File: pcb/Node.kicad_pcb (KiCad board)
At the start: 4 copper layers, 50 x 50 mm, 164 parts, among them J1 XF2M-1415-1A, J10 BM08B-SRSS-TB, J11 BM04B-SRSS-TB, J13 SM04B-SRSS-TB, J14 BM03B-SRSS-TB, J2 USB_C_USB2.0_16P, J3 BM03B-SRSS-TB, J4 BM06B-SRSS-TB, J5 BM06B-SRSS-TB, J6 BM04B-SRSS-TB, J7 BM06B-SRSS-TB, J8 BM04B-SRSS-TB, J9 BM04B-SRSS-TB, Q1 MMBT2222A, SW1 EVQ-Q2B02W, SW2 EVQ-Q2B02W, U1 ESP32-S3-WROOM-1-N8R2, U2 LM66200DRLR, U3 USBLC6-2P6, U4 MCP23017T-E/ML, U6 LM66200DRLR, U7 AZ1084-3.3

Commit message: Updated worksheet template and logo
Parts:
- removed kibuzzard-683C4F07: G***, kibuzzard-683C4F07
- added kibuzzard-685EFB19: G***, kibuzzard-685EFB19, F.Cu at (98.5, 65.2)
- LOGO1: footprint CRGM Logos:FNWW Face 10mm -> CRGM Logos:CRGM Logo 5mm
- moved LOGO3 18.0 mm to (81.6, 65.0)
- moved LOGO1 9.38 mm to (100.1, 62.7)
- moved LOGO2 7.61 mm to (89.4, 68.4)
- moved LOGO4 0.21 mm to (101.8, 61.9)

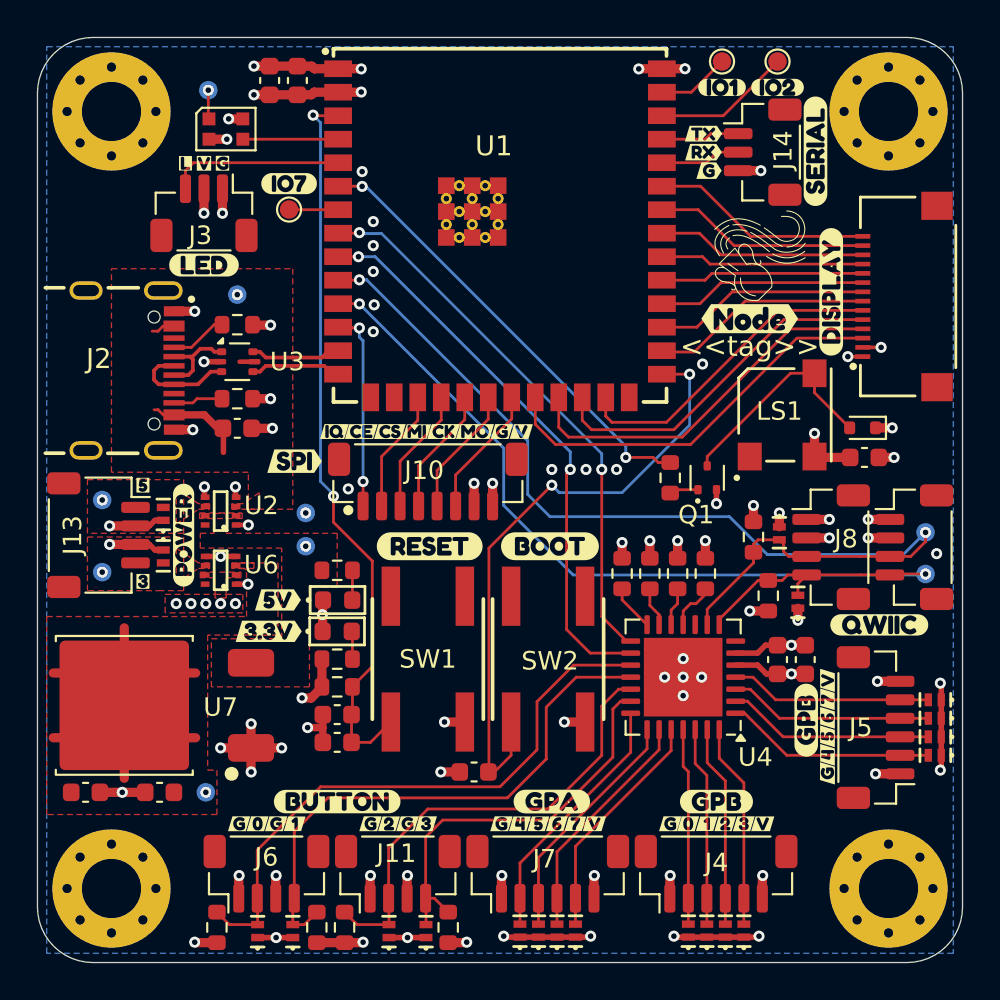
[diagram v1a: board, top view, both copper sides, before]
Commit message: Fixed footprint for Buzzer, XFC, USB ESD, and Power Switcher
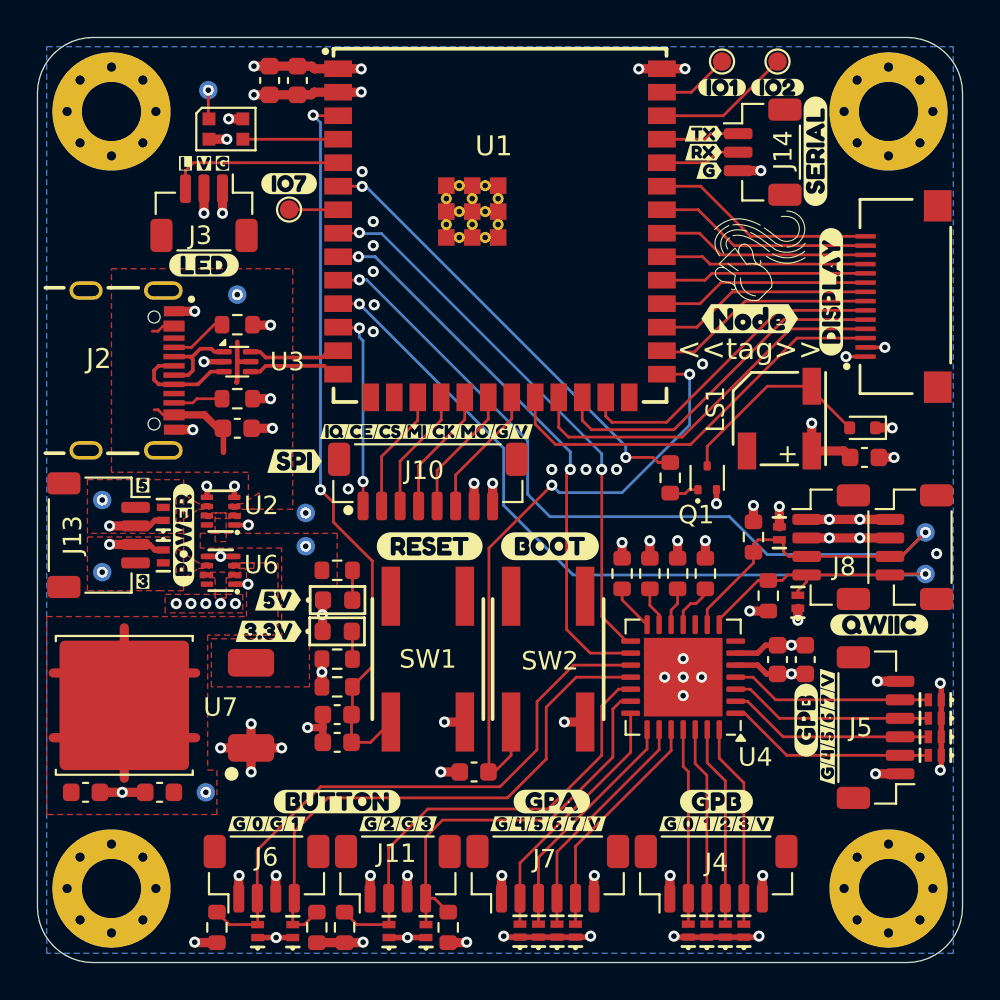
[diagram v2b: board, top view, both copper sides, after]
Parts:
- J1: footprint CRGM Connector:XF2C_1415-1A -> CRGM Connector:XF2M-1415-1A
- LS1: footprint CRG Makes:CMT050275SMTTR -> CRG Makes:FUET-5025
- moved LS1 0.36 mm to (100.1, 70.6)
- moved J1 0.35 mm to (106.7, 64.0)
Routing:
- net GND: track 89.5 -> 92.8 mm
- net USB_5V: track 7.54 -> 9.88 mm
- net +3.3V: track 35.3 -> 37.1 mm
- net /Peripherals/BUZZ_GND: track 11.9 -> 11.2 mm

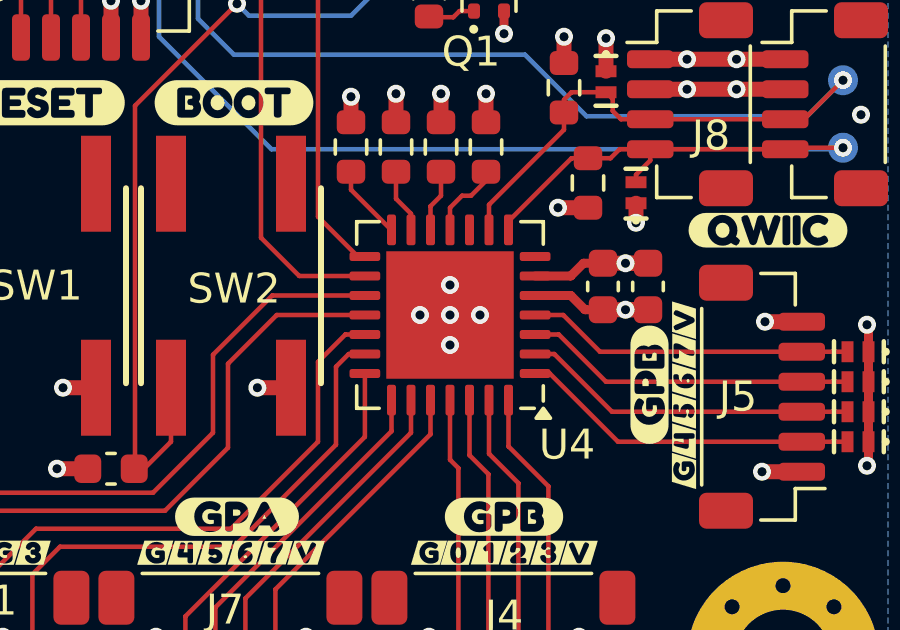
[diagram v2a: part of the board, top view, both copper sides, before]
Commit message: Moved termal vias.
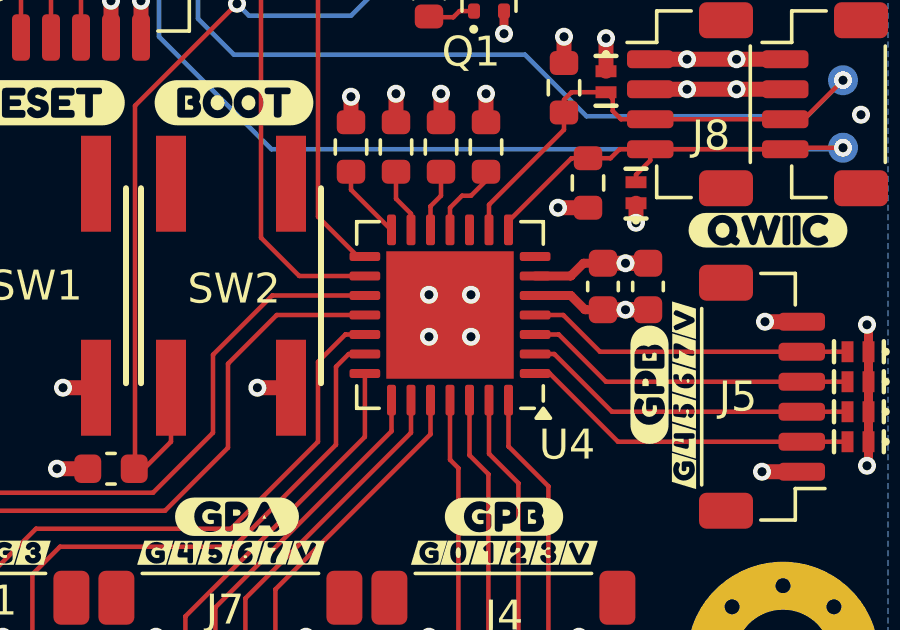
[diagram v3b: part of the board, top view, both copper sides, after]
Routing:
- net GND: track 92.8 -> 88.8 mm, vias 74 -> 73
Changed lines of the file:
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@@
 	)
 	(segment
-		(start 94.9 84.57564)
-		(end 94.9 83.57564)
-		(width 0.1524)
-		(layer "F.Cu")
-		(net 1)
-	)
-	(segment
 		(start 71.9 98.65)
 		(end 73.8 98.65)
@@
 	)
 	(segment
-		(start 94.9 84.57564)
-		(end 93.9 84.57564)
-		(width 0.1524)
-		(layer "F.Cu")
-		(net 1)
-	)
-	(segment
 		(start 72.88 96.525)
 		(end 72.88 95.32)
@@
 	)
 	(segment
-		(start 94.9 84.57564)
-		(end 95.9 84.57564)
-		(width 0.1524)
-		(layer "F.Cu")
-		(net 1)
-	)
-	(segment
 		(start 70 58.175)
 		(end 70 59.5)
@@
 	)
 	(segment
-		(start 94.9 84.57564)
-		(end 94.9 85.57564)
-		(width 0.1524)
-		(layer "F.Cu")
-		(net 1)
-	)
-	(segment
 		(start 79.98 96.525)
 		(end 79.98 95.32)
@@
 	)
 	(via
-		(at 93.9 84.57564)
+		(at 94.2 85.3)
 		(size 0.6)
 		(drill 0.3)
@@
 	)
 	(via
-		(at 94.9 83.57564)
+		(at 94.2 83.9)
 		(size 0.6)
 		(drill 0.3)
@@
 	)
 	(via
-		(at 94.9 84.57564)
-		(size 0.6)
-		(drill 0.3)
-		(layers "F.Cu" "B.Cu")
-		(net 1)
-	)
-	(via
 		(at 78.15 65.9)
 		(size 0.6)
@@
 	)
 	(via
-		(at 95.9 84.57564)
+		(at 95.6 83.9)
 		(size 0.6)
 		(drill 0.3)
@@
 	)
 	(via
-		(at 94.9 85.57564)
+		(at 95.6 85.3)
 		(size 0.6)
 		(drill 0.3)
@@
 		(polygon
 			(pts
-				(xy 69.55 76.8) (xy 70.2 76.8) (xy 70.2 76.8) (xy 76.2 76.8) (xy 76.2 79.7) (xy 74.7 79.7) (xy 74.7 85.1)
-				(xy 69.4 85.1) (xy 69.4 82.5) (xy 73.2 82.5) (xy 73.2 77.6) (xy 68.8 77.6) (xy 68.8 76.8) (xy 69.55 76.8)
+				(xy 69.55 76.8) (xy 70.2 76.8) (xy 76.2 76.8) (xy 76.2 79.7) (xy 74.7 79.7) (xy 74.7 85.1) (xy 69.4 85.1)
+				(xy 69.4 82.5) (xy 73.2 82.5) (xy 73.2 77.6) (xy 68.8 77.6) (xy 68.8 76.8)
 			)
 		)

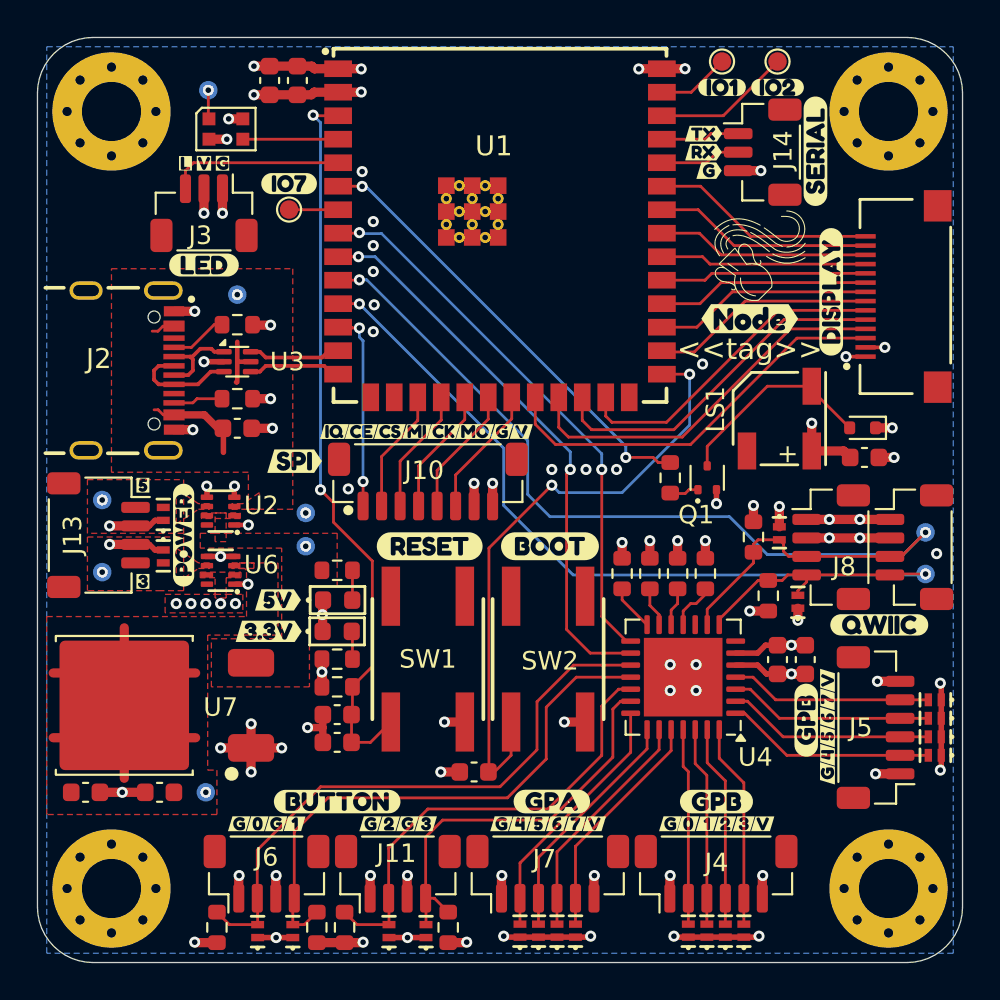
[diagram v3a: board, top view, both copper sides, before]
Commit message: Updated PCB for DFM
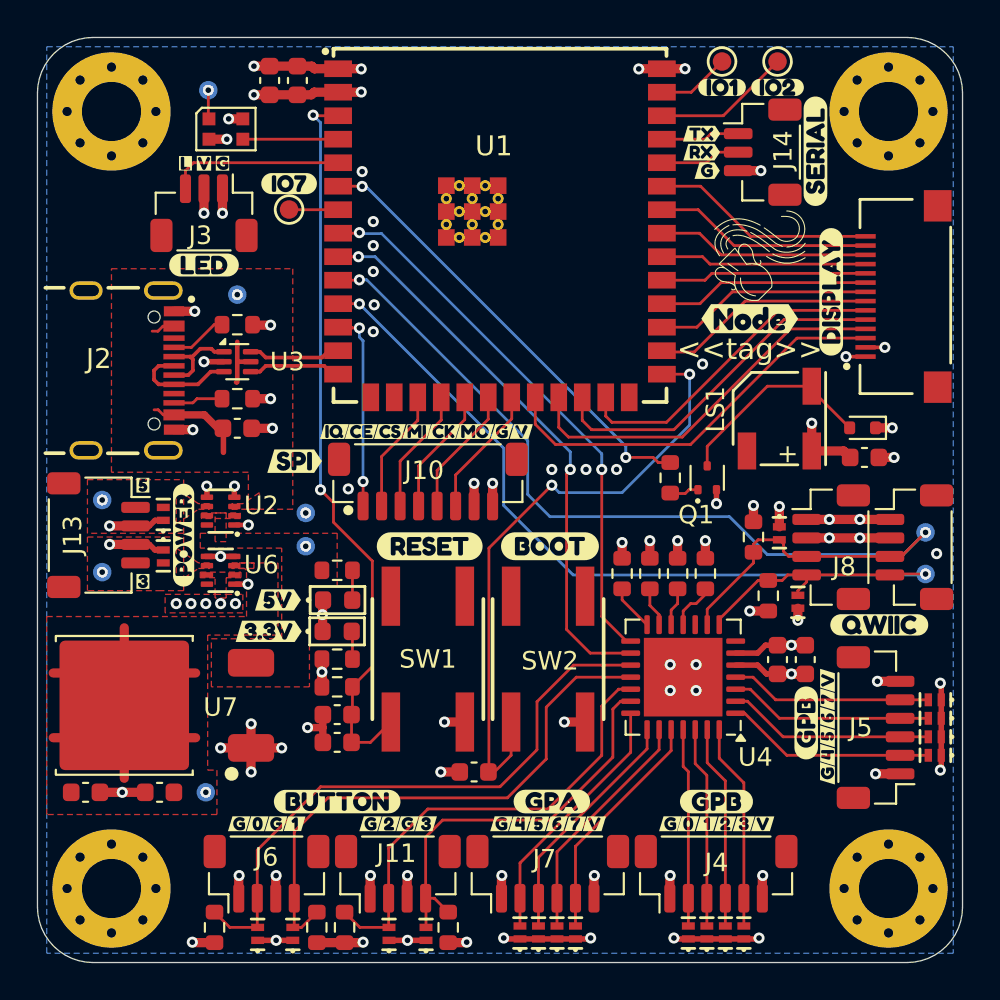
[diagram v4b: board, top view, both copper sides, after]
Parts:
- moved D12 0.15 mm to (71.9, 98.5)
- moved D13 0.15 mm to (73.8, 98.5)
- moved D14 0.15 mm to (79.0, 98.5)
- moved D15 0.15 mm to (81.0, 98.5)
- moved kibuzzard-6814212B 0.15 mm to (101.5, 87.0)
- moved R14 0.13 mm to (69.6, 98.1)
- moved D16 0.10 mm to (86.1, 98.4)
- moved D17 0.10 mm to (87.1, 98.4)
- moved D18 0.10 mm to (88.1, 98.4)
- moved D19 0.10 mm to (89.1, 98.4)
- moved D4 0.10 mm to (95.2, 98.4)
- moved D5 0.10 mm to (96.2, 98.4)
- moved D6 0.10 mm to (97.2, 98.4)
- moved D7 0.10 mm to (98.2, 98.4)
- moved kibuzzard-68574A7C 0.10 mm to (96.2, 57.2)
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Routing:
- net I2C_SDA: track 56.0 -> 55.4 mm
- net D_N: track 5.01 -> 4.50 mm
